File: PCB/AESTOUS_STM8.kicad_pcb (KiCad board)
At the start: 2 copper layers, 23 parts, among them J1 Conn_01x04_Male, J2 Conn_01x04_Male, J3 USB_B_Micro, U1 STM8S003F3P

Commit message: new version
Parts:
- removed the C7 at (130.2, 82.2)
- removed R4: 0603WAF1002T5E, Resistor_SMD:R_0603_1608Metric_Pad1.05x0.95mm_HandSolder
- added C12: CL10A105KB8NNNC, Capacitor_SMD:C_0603_1608Metric_Pad1.05x0.95mm_HandSolder, F.Cu at (116.0, 135.0)
- added C13: CL10A105KB8NNNC, Capacitor_SMD:C_0603_1608Metric_Pad1.05x0.95mm_HandSolder, F.Cu at (120.2, 143.8)
- added C5: CL10A105KB8NNNC, Capacitor_SMD:C_0603_1608Metric_Pad1.05x0.95mm_HandSolder, F.Cu at (196.5, 140.4)
- added Q1: NCE2060K, Package_TO_SOT_SMD:TO-252-2, F.Cu at (180.3, 142.8)
- added R2: 0603WAF2700T5E, Resistor_SMD:R_0603_1608Metric_Pad1.05x0.95mm_HandSolder, F.Cu at (174.5, 146.4)
- added R6: 0603WAF1002T5E, Resistor_SMD:R_0603_1608Metric_Pad1.05x0.95mm_HandSolder, F.Cu at (121.0, 138.5)
- added R7: 0603WAF1002T5E, Resistor_SMD:R_0603_1608Metric_Pad1.05x0.95mm_HandSolder, F.Cu at (117.9, 136.8)
- added R8: 0603WAF1002T5E, Resistor_SMD:R_0603_1608Metric_Pad1.05x0.95mm_HandSolder, F.Cu at (121.0, 146.1)
- added TH3: NCP15XH103F03RC, Resistor_SMD:R_0603_1608Metric_Pad1.05x0.95mm_HandSolder, F.Cu at (168.2, 147.4)
- C1, C10, C11, C2, C3, C4, C6, C8, C9: value CL10B105KA8NNNC -> CL10A105KB8NNNC
- C7: renamed from C5; value 0603CG101J500NT -> CL10C101JB8NNNC
- J1, J2: value Conn_01x04_Male -> Conn_01x04
- R3: value 0603WAF1002T5E -> 0603WAF3002T5E
- TH1: moved to B.Cu
- moved J3 97.9 mm to (195.1, 146.3)
- moved C2 89.8 mm to (189.2, 141.2), turned to 180 degrees
- moved C7 72.8 mm to (108.5, 145.1), turned to 270 degrees
- moved C4 72.1 mm to (106.2, 145.1), turned to 270 degrees
- moved R3 70.1 mm to (171.1, 146.6), turned to 90 degrees
- moved C10 67.9 mm to (127.1, 147.1), turned to 90 degrees
- moved C6 66.9 mm to (107.3, 142.5), turned to 180 degrees
- moved FB1 63.4 mm to (135.8, 148.0)
- moved C1 62.7 mm to (104.5, 145.1), turned to 270 degrees
- moved C9 62.0 mm to (129.3, 147.1), turned to 90 degrees
- moved C11 59.5 mm to (121.0, 140.1)
- moved U1 54.6 mm to (114.1, 141.8)
- moved C8 54.6 mm to (114.0, 146.5)
- moved R1 54.2 mm to (107.1, 139.5), turned to 270 degrees
- moved C3 48.9 mm to (104.5, 140.4), turned to 180 degrees
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- renumbered R2 to R5
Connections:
- C1 pad 1: VDD -> +5VD
- C1 pad 2: GND -> 0
- C10 pad 1: +5V -> +5VD
- C10 pad 2: GND -> 0
- C11 pad 2: GND -> 0
- C2 pad 1: VDD -> Net-(Q1-Pad2)
- C2 pad 2: GND -> 0
- C3 pad 1: +5V -> /NRST
- C3 pad 2: GND -> 0
- C4 pad 1: +5V -> +5VD
- C4 pad 2: GND -> 0
- C6 pad 1: /NRST -> Net-(C6-Pad1)
- C6 pad 2: GND -> 0
- C7 pad 1: +5V -> +5VD
- C7 pad 2: GND -> 0
- C8 pad 1: +5V -> +5VD
- C8 pad 2: GND -> 0
- C9 pad 1: /ADC_IN4 -> +5VD
- C9 pad 2: GND -> 0
- D1 pad 1: GND -> 0
- FB1 pad 1: +5V -> +5VD
- J1 pad 1: +5V -> /NRST
- J1 pad 2: /UART_TX -> 0
- J1 pad 3: /UART_RX -> /SWIM
- J1 pad 4: GND -> +5VD
- J2 pad 1: +5V -> 0
- J2 pad 2: /SWIM -> /UART_RX
- J2 pad 3: GND -> /UART_TX
- J2 pad 4: /NRST -> +5VD
- J3 pad 1: VDD -> Net-(Q1-Pad2)
- J3 pad 5: GND -> 0
- J3 pad 6: GND -> 0
- R1 pad 1: +5V -> +5VD
- R3 pad 1: +5V -> 0
- R3 pad 2: /ADC_IN4 -> /TIM1_CH1
- TH1 pad 1: /ADC_IN4 -> /ADC_IN3
- TH1 pad 2: GND -> 0
- TH2 pad 1: /ADC_IN3 -> /ADC_IN4
- TH2 pad 2: GND -> 0
- U1 pad 7: GND -> 0
- U1 pad 8: Net-(C7-Pad1) -> Net-(C6-Pad1)
- U1 pad 9: +5V -> +5VD
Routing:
- net Net-(Q1-Pad2): track 0.00 -> 5653.8 mm, vias 0 -> 45
- net +5VD: track 0.00 -> 169.5 mm, vias 0 -> 2
- net /DM: track 0.00 -> 100.1 mm, vias 0 -> 2
- net /DP: track 0.00 -> 98.6 mm, vias 0 -> 2
- net /UART_RX: track 0.00 -> 95.7 mm, vias 0 -> 1
- net /UART_TX: track 0.00 -> 95.1 mm, vias 0 -> 1
- net /ADC_IN4: track 0.00 -> 87.7 mm
- net /LED: track 0.00 -> 85.2 mm
- net /NRST: track 0.00 -> 78.7 mm
- net /SWIM: track 0.00 -> 77.8 mm
- net /TIM1_CH1: track 0.00 -> 58.8 mm
- net /ADC_IN3: track 0.00 -> 58.0 mm, vias 0 -> 2
- net VDD: track 0.00 -> 57.4 mm
- net /ADC_IN2: track 0.00 -> 55.0 mm
- net 0: track 0.00 -> 35.3 mm, vias 0 -> 261
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- added copper zone on B.Cu, net 0
- added copper zone on F.Cu, net 0
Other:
- board outline added: 100 x 100 mm
- net class Default: clearance 0.2 -> 0.3; trace_width 0.25 -> 0.3; via_dia 0.8 -> 0.9; via_drill 0.4 -> 0.6
- rule trace_clearance: 0.2 -> 0.3
- rule trace_min: 0.2 -> 0.3

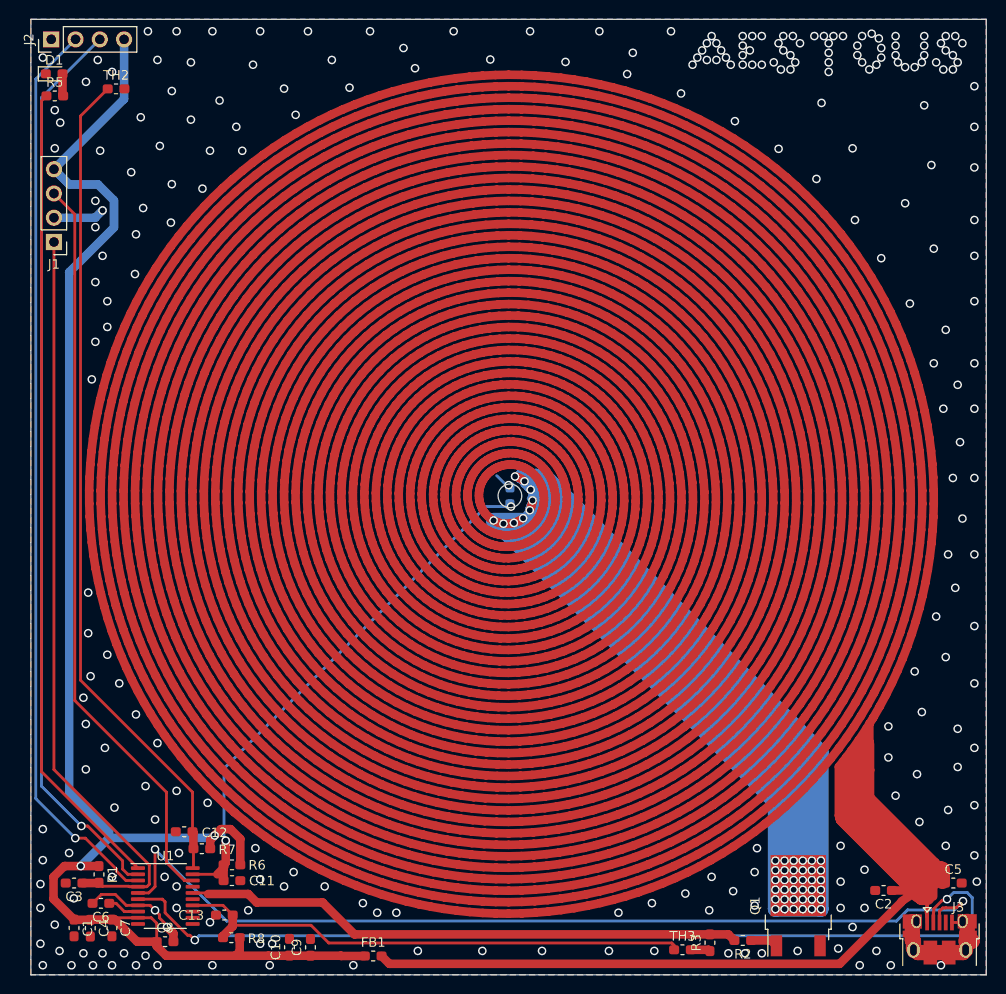
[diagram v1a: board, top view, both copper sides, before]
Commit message: Add iar project and update PCB
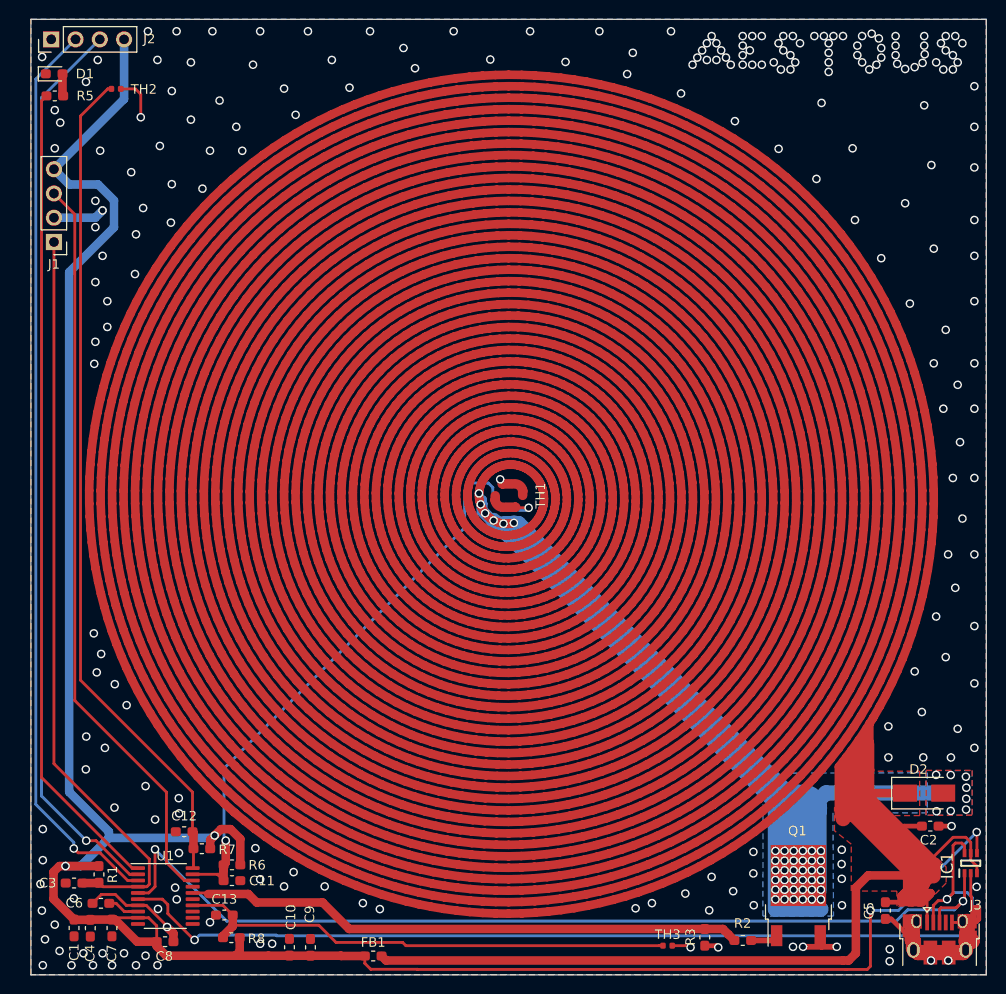
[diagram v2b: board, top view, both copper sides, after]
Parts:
- added D2: SS34, Diode_SMD:D_SMA, F.Cu at (193.5, 131.0)
- added IC1: SMF05CT1G, SamacSys_Parts:SOT65P210X110-6N, F.Cu at (198.4, 138.3)
- C1, C10, C11, C12, C13, C2, C3, C4, C5, C6, C8, C9: value CL10A105KB8NNNC -> 1UF 50V
- C7: value CL10C101JB8NNNC -> 100PF 50V
- R1, R6, R7, R8: value 0603WAF1002T5E -> 10 KOHMS ±1%
- R2: value 0603WAF2700T5E -> 270 OHMS ±1%
- R3: value 0603WAF3002T5E -> 30 KOHMS ±1%
- R5: value 0603WAF3300T5E -> 330 OHMS ±1%
- TH1: value NCP15XH103F03RC -> NTC 10KOHMS ±1%; footprint Resistor_SMD:R_0603_1608Metric_Pad1.05x0.95mm_HandSolder -> SamacSys_Parts:0403_inside; moved to F.Cu
- TH2, TH3: value NCP15XH103F03RC -> NTC 10KOHMS ±1%; footprint Resistor_SMD:R_0603_1608Metric_Pad1.05x0.95mm_HandSolder -> Resistor_SMD:R_0402_1005Metric
- moved C2 8.32 mm to (194.1, 134.4), turned to 0 degrees
- moved C5 7.67 mm to (189.4, 143.3), turned to 270 degrees
- moved TH3 1.61 mm to (166.6, 147.0)
- moved Q1 1.06 mm to (180.3, 141.7)
- moved R3 0.78 mm to (170.5, 146.1)
- moved TH1 0.11 mm to (150.0, 99.8), turned to 270 degrees
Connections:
- C2 pad 1: Net-(Q1-Pad2) -> VDD
- C5 pad 1: Net-(Q1-Pad2) -> VDD
- J3 pad 1: Net-(Q1-Pad2) -> VDD
- Q1 pad 2: Net-(Q1-Pad2) -> VDD
- TH1 pad 1: /ADC_IN3 -> 0
- TH1 pad 2: 0 -> /ADC_IN3
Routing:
- net Net-(Q1-Pad2): track 5653.8 -> 0.00 mm, vias 45 -> 0
- net VDD: track 57.4 -> 5561.1 mm, vias 0 -> 50
- net +5VD: track 169.5 -> 247.9 mm, vias 2 -> 4
- net 0: track 35.3 -> 61.6 mm, vias 261 -> 237
- net /ADC_IN3: track 58.0 -> 68.1 mm
- net /DM: track 100.1 -> 108.4 mm
- net /DP: track 98.6 -> 101.7 mm
- net /ADC_IN2: track 55.0 -> 53.4 mm
- net /UART_RX: track 95.7 -> 96.2 mm
- added copper zone on B.Cu, net VDD
- added copper zone on F.Cu, net VDD
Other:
- outline, holes or cut-outs redrawn
